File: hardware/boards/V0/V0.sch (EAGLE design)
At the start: 149 parts, among them IC2 TPS6300, J12 3.5mm TRRS Jack, J2 HIROSE_DM3BT-DSF-PEJSHIROSE_D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, J3 MOLEX_105450-0101MOLEX_105450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, Q2 ON_SEMI_MMBT5551LT1GON_SEMI_M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, U1 VS1053-L, U2 MICROCHIP_MCP73831T-2ATI-OTMI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, X3 FH12-45S-0.5SH

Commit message: checkpoint
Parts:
- C24, C25: device rcl:CPOL-USC/6032-28R -> rcl:C-USC0402
- C34: device rcl:C-USC1206 -> rcl:C-USC0402
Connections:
- net GND: now also C24.2, C25.2; no longer C24.-, C25.-
- net V3P3: now also C24.1, C25.1; no longer C24.+, C25.+
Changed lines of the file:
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@@
 <?xml version="1.0" encoding="utf-8"?>
 <!DOCTYPE eagle SYSTEM "eagle.dtd">
-<eagle version="9.3.0">
+<eagle version="9.4.0">
 <drawing>
 <settings>
@@
 <part name="GND20" library="supply1" library_urn="urn:adsk.eagle:library:371" deviceset="GND" device=""/>
 <part name="GND23" library="supply1" library_urn="urn:adsk.eagle:library:371" deviceset="GND" device=""/>
-<part name="C24" library="rcl" library_urn="urn:adsk.eagle:library:334" deviceset="CPOL-US" device="C/6032-28R" package3d_urn="urn:adsk.eagle:package:23415/2" value="4.7uF"/>
-<part name="C25" library="rcl" library_urn="urn:adsk.eagle:library:334" deviceset="CPOL-US" device="C/6032-28R" package3d_urn="urn:adsk.eagle:package:23415/2" value="0.1uF"/>
+<part name="C24" library="rcl" library_urn="urn:adsk.eagle:library:334" deviceset="C-US" device="C0402" package3d_urn="urn:adsk.eagle:package:23626/2" value="4.7uF"/>
+<part name="C25" library="rcl" library_urn="urn:adsk.eagle:library:334" deviceset="C-US" device="C0402" package3d_urn="urn:adsk.eagle:package:23626/2" value="0.1uF"/>
 <part name="GND24" library="supply1" library_urn="urn:adsk.eagle:library:371" deviceset="GND" device=""/>
 <part name="GND25" library="supply1" library_urn="urn:adsk.eagle:library:371" deviceset="GND" device=""/>
@@
 <part name="GND43" library="supply1" library_urn="urn:adsk.eagle:library:371" deviceset="GND" device=""/>
 <part name="R50" library="rcl" library_urn="urn:adsk.eagle:library:334" deviceset="R-US_" device="R0402" package3d_urn="urn:adsk.eagle:package:23547/3" value="10k"/>
-<part name="C34" library="rcl" library_urn="urn:adsk.eagle:library:334" deviceset="C-US" device="C1206" package3d_urn="urn:adsk.eagle:package:23618/2" value="0.1uF"/>
+<part name="C34" library="rcl" library_urn="urn:adsk.eagle:library:334" deviceset="C-US" device="C0402" package3d_urn="urn:adsk.eagle:package:23626/2" value="0.1uF"/>
 <part name="GND44" library="supply1" library_urn="urn:adsk.eagle:library:371" deviceset="GND" device=""/>
 <part name="GND45" library="supply1" library_urn="urn:adsk.eagle:library:371" deviceset="GND" device=""/>
@@
 </segment>
 <segment>
-<pinref part="C24" gate="G$1" pin="-"/>
+<pinref part="C24" gate="G$1" pin="2"/>
 <wire x1="-182.88" y1="20.32" x2="-182.88" y2="17.78" width="0.1524" layer="91"/>
 <pinref part="GND24" gate="1" pin="GND"/>
 </segment>
 <segment>
-<pinref part="C25" gate="G$1" pin="-"/>
+<pinref part="C25" gate="G$1" pin="2"/>
 <wire x1="-172.72" y1="20.32" x2="-172.72" y2="17.78" width="0.1524" layer="91"/>
 <pinref part="GND25" gate="1" pin="GND"/>
@@
 </segment>
 <segment>
-<pinref part="C25" gate="G$1" pin="+"/>
+<pinref part="C25" gate="G$1" pin="1"/>
 <wire x1="-172.72" y1="30.48" x2="-172.72" y2="27.94" width="0.1524" layer="91"/>
-<pinref part="C24" gate="G$1" pin="+"/>
+<pinref part="C24" gate="G$1" pin="1"/>
 <wire x1="-182.88" y1="27.94" x2="-182.88" y2="30.48" width="0.1524" layer="91"/>
 <label x="-190.5" y="33.02" size="1.778" layer="95"/>
@@
 packages will not be understood (or retained) with this version.
 </note>
-<note version="8.4" severity="warning">
-Since Version 8.4, EAGLE supports properties for SPICE simulation.
-Probes in schematics and SPICE mapping objects found in parts and library devices
-will not be understood with this version. Update EAGLE to the latest version
-for full support of SPICE simulation.
-</note>
 </compatibility>

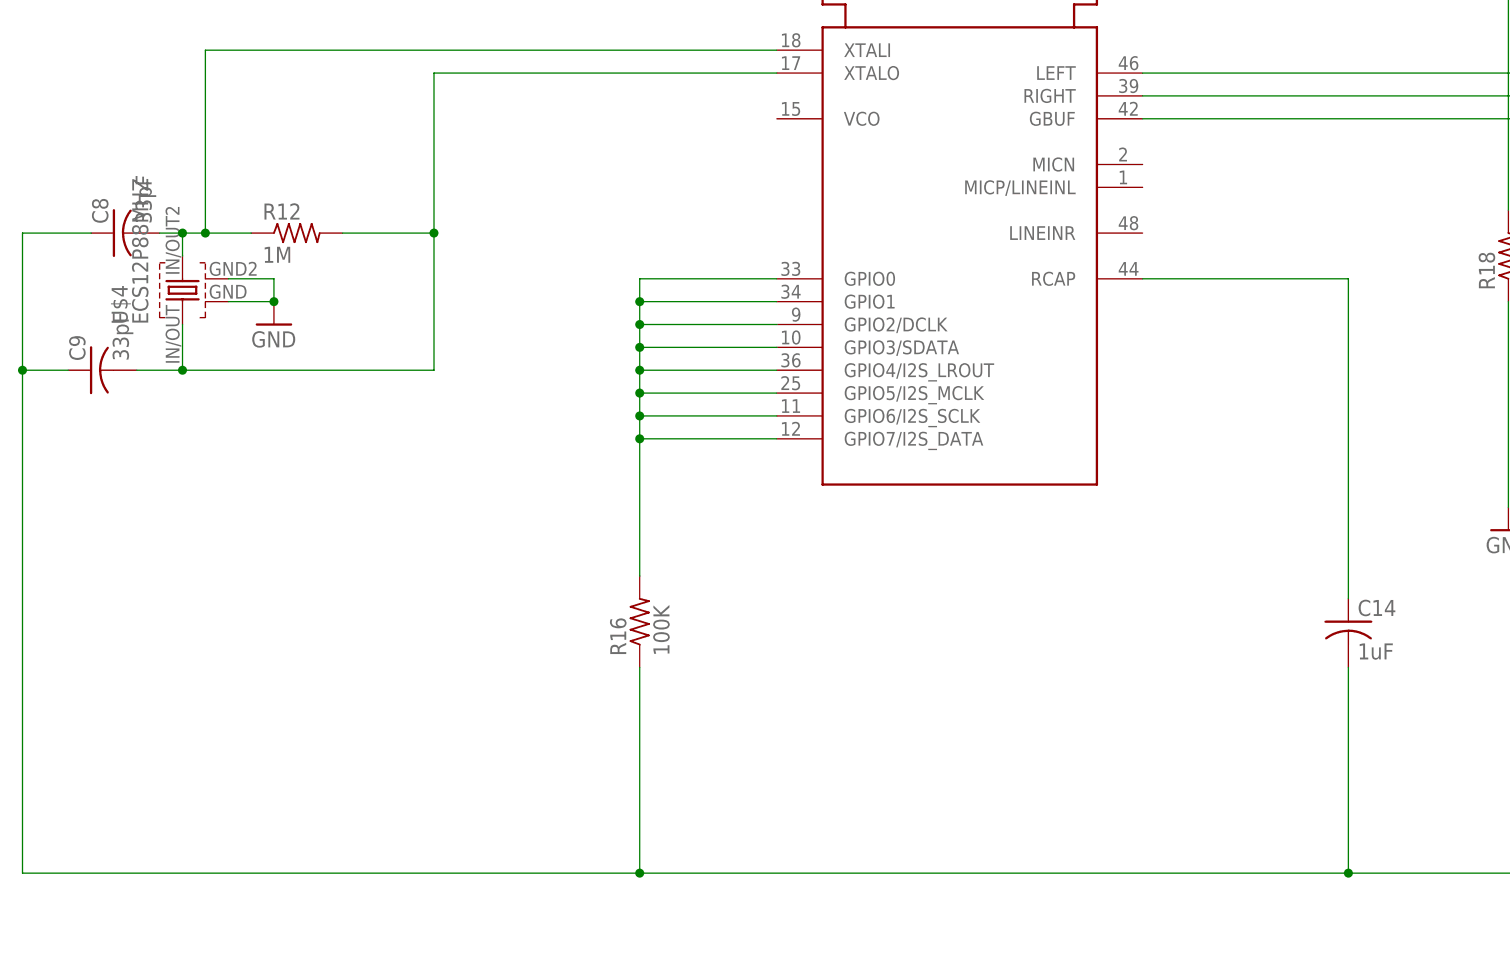
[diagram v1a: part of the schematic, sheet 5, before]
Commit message: swap VS1053 GPIO pull down resistors
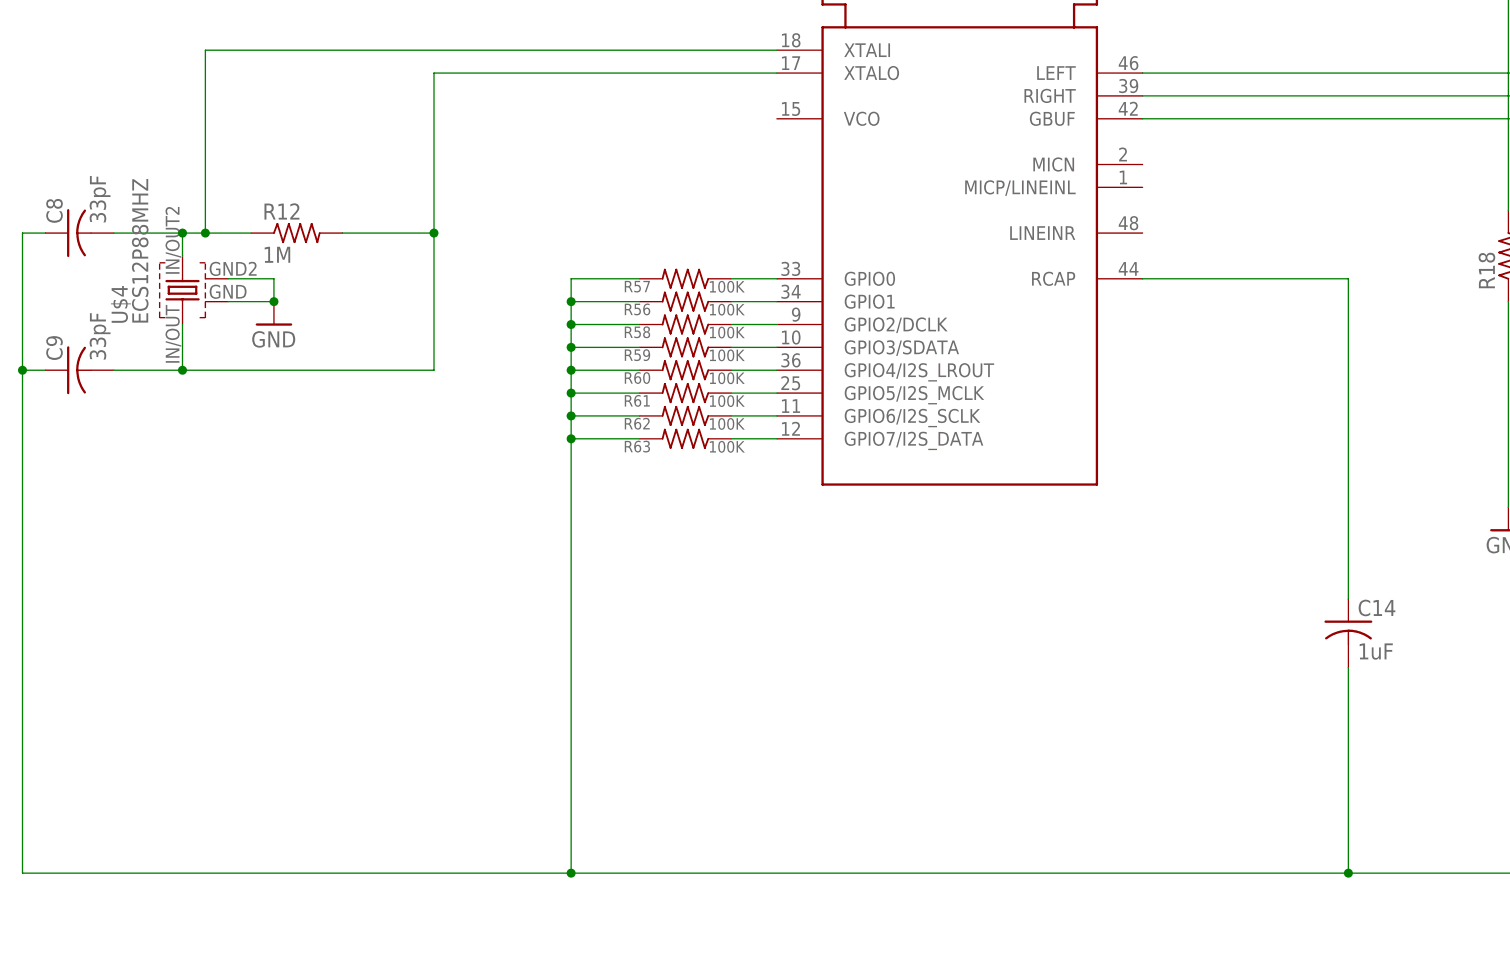
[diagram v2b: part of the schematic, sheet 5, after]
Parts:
- removed R16: 100K, rcl:R-US_R0402
- added R56, R57, R58, R59, R60, R61, R62, R63: 100K, rcl:R-US_R0402
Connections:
- new net N$13: R58.1, U1G$1.GPIO2/DCLK
- new net N$15: R59.1, U1G$1.GPIO3/SDATA
- new net N$17: R60.1, U1G$1.GPIO4/I2S_LROUT
- new net N$44: R62.1, U1G$1.GPIO6/I2S_SCLK
- new net N$45: R63.1, U1G$1.GPIO7/I2S_DATA
- new net N$7: R57.1, U1G$1.GPIO0
- new net N$9: R56.1, U1G$1.GPIO1
- net GND: now also R56.2, R57.2, R58.2, R59.2, R60.2, R61.2, R62.2, R63.2; no longer R16.1
- net N$38: now also R61.1; no longer R16.2, U1G$1.GPIO0, U1G$1.GPIO1, U1G$1.GPIO2/DCLK, U1G$1.GPIO3/SDATA, U1G$1.GPIO4/I2S_LROUT, U1G$1.GPIO6/I2S_SCLK, U1G$1.GPIO7/I2S_DATA
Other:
- moved on the sheet: C8, C9

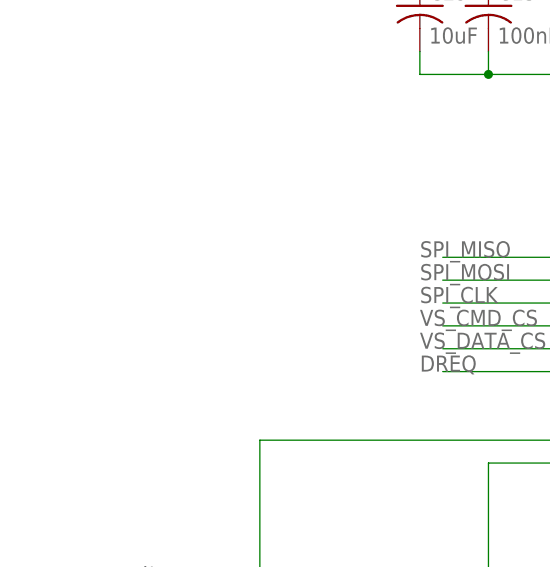
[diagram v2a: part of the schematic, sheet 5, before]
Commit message: add backup header pin block for the VS1053
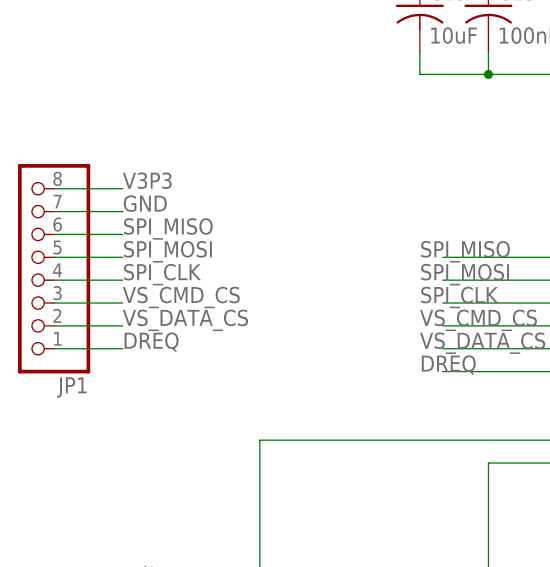
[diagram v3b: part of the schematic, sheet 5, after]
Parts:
- added JP1: (no value), adafruit:PINHD-1X8LOCK
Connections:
- net DREQ: now also JP1.1
- net GND: now also JP1.7
- net SPI_CLK: now also JP1.4
- net SPI_MISO: now also JP1.6
- net SPI_MOSI: now also JP1.5
- net V3P3: now also JP1.8
- net VS_CMD_CS: now also JP1.3
- net VS_DATA_CS: now also JP1.2
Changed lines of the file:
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@@
 <part name="R62" library="rcl" library_urn="urn:adsk.eagle:library:334" deviceset="R-US_" device="R0402" package3d_urn="urn:adsk.eagle:package:23547/3" value="100K"/>
 <part name="R63" library="rcl" library_urn="urn:adsk.eagle:library:334" deviceset="R-US_" device="R0402" package3d_urn="urn:adsk.eagle:package:23547/3" value="100K"/>
+<part name="JP1" library="adafruit" library_urn="urn:adsk.eagle:library:420" deviceset="PINHD-1X8" device="LOCK" package3d_urn="urn:adsk.eagle:package:6240709/1"/>
 </parts>
 <sheets>
@@
 <attribute name="VALUE" x="-27.94" y="-42.164" size="1.27" layer="96"/>
 </instance>
+<instance part="JP1" gate="G$1" x="-109.22" y="20.32" smashed="yes" rot="R180">
+<attribute name="NAME" x="-102.87" y="9.525" size="1.778" layer="95" rot="R180"/>
+<attribute name="VALUE" x="-102.87" y="35.56" size="1.778" layer="96" rot="R180"/>
+</instance>
 </instances>
 <busses>
@@
 <junction x="-76.2" y="-25.4"/>
 </segment>
+<segment>
+<pinref part="JP1" gate="G$1" pin="7"/>
+<wire x1="-106.68" y1="27.94" x2="-99.06" y2="27.94" width="0.1524" layer="91"/>
+<label x="-99.06" y="27.94" size="1.778" layer="95"/>
+</segment>
 </net>
 <net name="N$4" class="0">
@@
 <wire x1="-15.24" y1="101.6" x2="-15.24" y2="78.74" width="0.1524" layer="91"/>
 </segment>
+<segment>
+<pinref part="JP1" gate="G$1" pin="8"/>
+<wire x1="-106.68" y1="30.48" x2="-99.06" y2="30.48" width="0.1524" layer="91"/>
+<label x="-99.06" y="30.48" size="1.778" layer="95"/>
+</segment>
 </net>
 <net name="N$41" class="0">
@@
 <label x="-66.04" y="22.86" size="1.778" layer="95"/>
 </segment>
+<segment>
+<pinref part="JP1" gate="G$1" pin="6"/>
+<wire x1="-106.68" y1="25.4" x2="-99.06" y2="25.4" width="0.1524" layer="91"/>
+<label x="-99.06" y="25.4" size="1.778" layer="95"/>
+</segment>
 </net>
 <net name="SPI_MOSI" class="0">
@@
 <label x="-66.04" y="20.32" size="1.778" layer="95"/>
 </segment>
+<segment>
+<pinref part="JP1" gate="G$1" pin="5"/>
+<wire x1="-106.68" y1="22.86" x2="-99.06" y2="22.86" width="0.1524" layer="91"/>
+<label x="-99.06" y="22.86" size="1.778" layer="95"/>
+</segment>
 </net>
 <net name="SPI_CLK" class="0">
@@
 <label x="-66.04" y="17.78" size="1.778" layer="95"/>
 </segment>
+<segment>
+<pinref part="JP1" gate="G$1" pin="4"/>
+<wire x1="-106.68" y1="20.32" x2="-99.06" y2="20.32" width="0.1524" layer="91"/>
+<label x="-99.06" y="20.32" size="1.778" layer="95"/>
+</segment>
 </net>
 <net name="VS_CMD_CS" class="0">
@@
 <label x="-66.04" y="15.24" size="1.778" layer="95"/>
 </segment>
+<segment>
+<pinref part="JP1" gate="G$1" pin="3"/>
+<wire x1="-106.68" y1="17.78" x2="-99.06" y2="17.78" width="0.1524" layer="91"/>
+<label x="-99.06" y="17.78" size="1.778" layer="95"/>
+</segment>
 </net>
 <net name="VS_DATA_CS" class="0">
@@
 <label x="-66.04" y="12.7" size="1.778" layer="95"/>
 </segment>
+<segment>
+<pinref part="JP1" gate="G$1" pin="2"/>
+<wire x1="-106.68" y1="15.24" x2="-99.06" y2="15.24" width="0.1524" layer="91"/>
+<label x="-99.06" y="15.24" size="1.778" layer="95"/>
+</segment>
 </net>
 <net name="DREQ" class="0">
@@
 <label x="-66.04" y="10.16" size="1.778" layer="95"/>
 </segment>
-</net>
+<segment>
+<pinref part="JP1" gate="G$1" pin="1"/>
+<wire x1="-106.68" y1="12.7" x2="-99.06" y2="12.7" width="0.1524" layer="91"/>
+<label x="-99.06" y="12.7" size="1.778" layer="95"/>
+</segment>
+</net>
